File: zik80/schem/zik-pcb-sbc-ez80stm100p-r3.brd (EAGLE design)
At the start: 149.8 x 98.7 mm, 96 parts, among them IC1 7432N, IC2 7404N

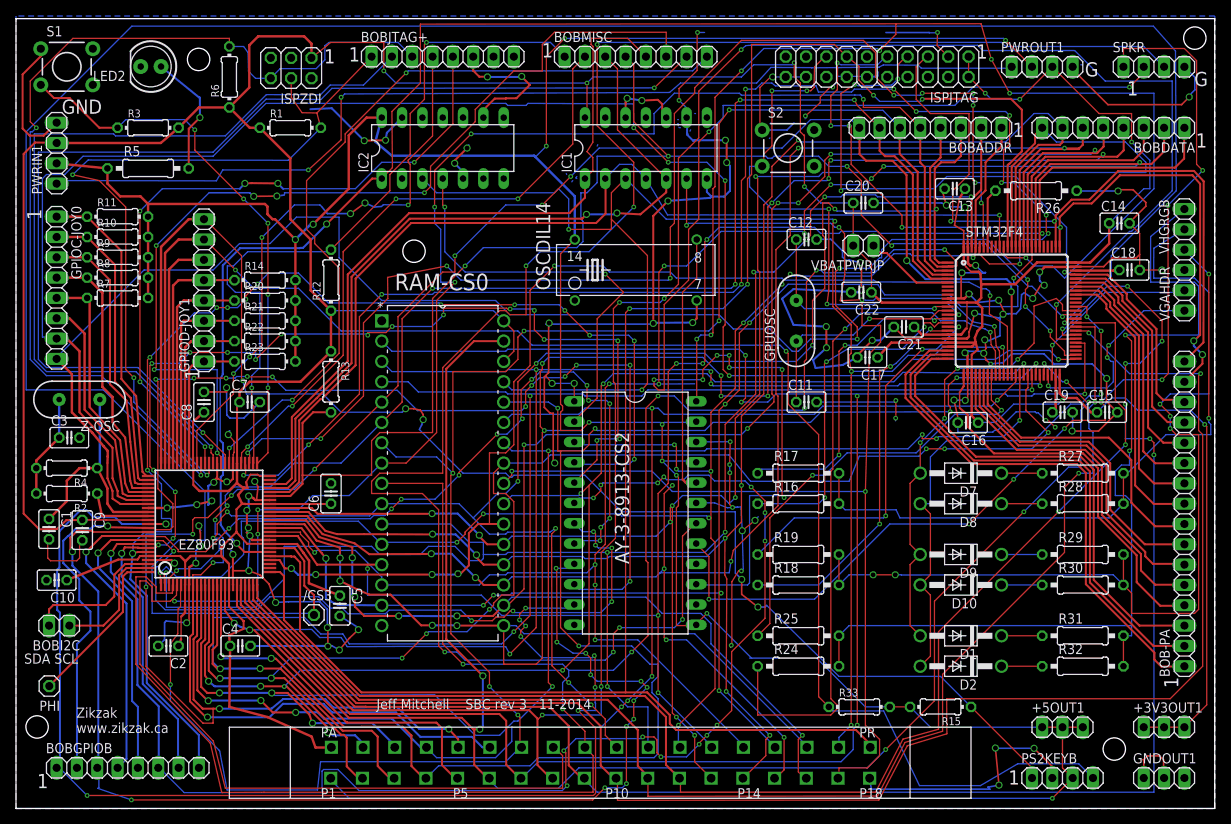
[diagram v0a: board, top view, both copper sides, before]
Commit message: Final(?) rev3 zikzak sbc; created brand new zok atmega644 BoB design and board, WIP
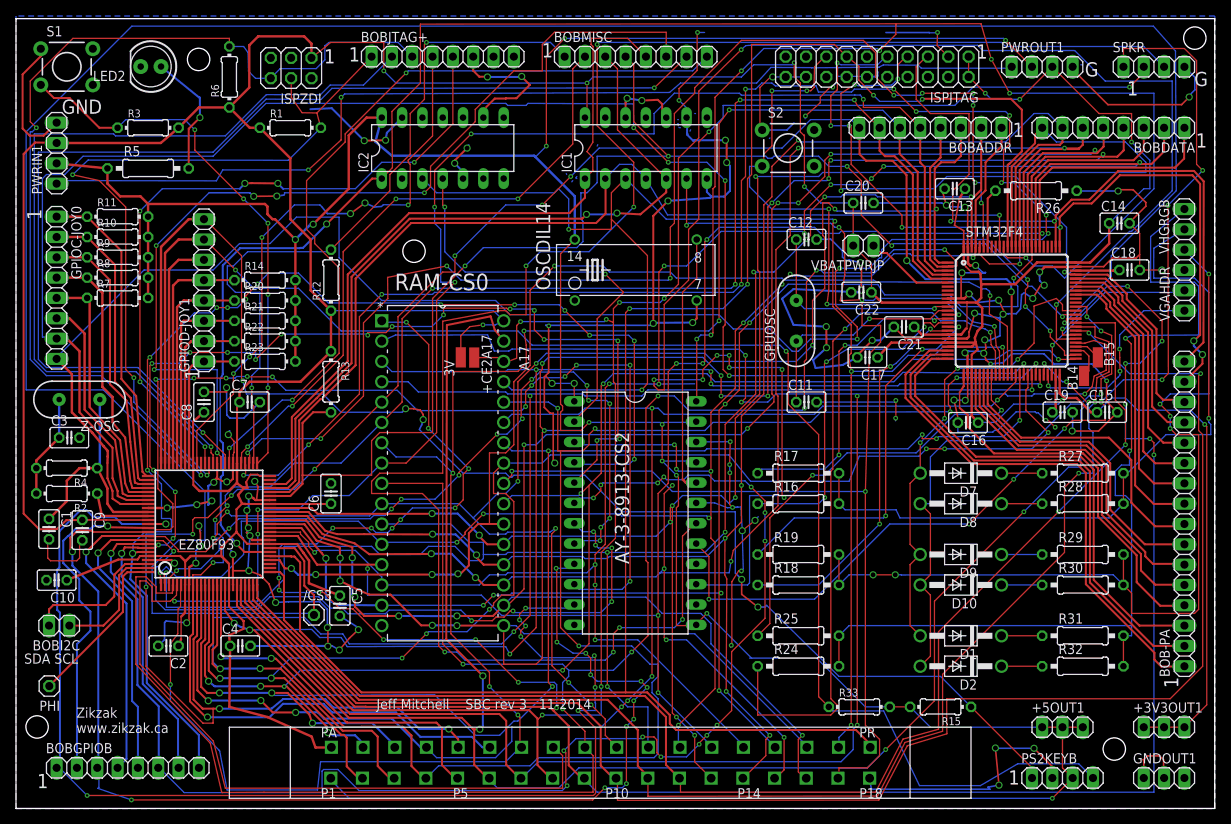
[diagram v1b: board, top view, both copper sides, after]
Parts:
- added +CE2A17, 3V, B14, B15: WIREPADSMD1,27-254, wirepad:SMD1,27-2,54
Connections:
- net +3V3: now also 3V.1; no longer RAM-CS0.30
- net A17: now also +CE2A17.1, RAM-CS0.30
- net A18: now also RAM-CS0.1
- net PB14: now also B14.1
- net PB15: now also B15.1
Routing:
- net A18: track 212.0 -> 315.2 mm, vias 7 -> 22
- net A17: track 251.7 -> 273.9 mm, vias 6 -> 8
- net A15: track 218.2 -> 224.2 mm
- net A16: track 240.9 -> 245.8 mm
- net PB14: track 0.00 -> 4.67 mm
- net PB15: track 0.00 -> 3.33 mm
- net N$28: track 228.4 -> 231.3 mm
- net +3V3: track 655.8 -> 658.3 mm, vias 9 -> 10
- net A20: track 168.3 -> 170.5 mm
- net PC7: track 67.2 -> 68.9 mm
- net A5: track 239.2 -> 240.2 mm
- net PB10: track 26.3 -> 25.5 mm
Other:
- board text added: "A17"

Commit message: Finished up zok atmega bob rev1, and zikzak sbc rev3
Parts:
- renumbered S1 to EZ80-RESET, S2 to STM-RESET
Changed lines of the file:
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@@
 <attribute name="OC_FARNELL" value="unknown" x="100.33" y="10.16" size="1.778" layer="27" display="off"/>
 </element>
-<element name="S1" library="SparkFun-Electromechanical" package="TACTILE-PTH" value="SWITCH-MOMENTARY-2PTH" x="6.35" y="92.71"/>
+<element name="EZ80-RESET" library="SparkFun-Electromechanical" package="TACTILE-PTH" value="SWITCH-MOMENTARY-2PTH" x="6.35" y="92.71"/>
 <element name="R3" library="rcl" package="0204/7" value="10K" x="16.51" y="85.09"/>
 <element name="R2" library="rcl" package="0204/7" value="220 O" x="6.35" y="39.37" rot="R180"/>
@@
 <element name="C18" library="rcl" package="C025-025X050" value="2.2uF" x="139.192" y="67.31"/>
 <element name="C19" library="rcl" package="C025-025X050" value="2.2uF" x="130.81" y="49.53"/>
-<element name="S2" library="SparkFun-Electromechanical" package="TACTILE-PTH" value="SWITCH-MOMENTARY-2PTH" x="96.52" y="82.55"/>
+<element name="STM-RESET" library="SparkFun-Electromechanical" package="TACTILE-PTH" value="SWITCH-MOMENTARY-2PTH" x="96.52" y="82.55"/>
 <element name="VGAHDR" library="pinhead" package="1X06" value="" x="146.05" y="68.58" rot="R90"/>
 <element name="R16" library="rcl" package="0207/10" value="2K" x="97.79" y="38.1"/>
@@
 <contactref element="IC1" pad="7"/>
 <contactref element="IC2" pad="7"/>
-<contactref element="S1" pad="1"/>
+<contactref element="EZ80-RESET" pad="1"/>
 <contactref element="C1" pad="2"/>
 <contactref element="C3" pad="2"/>
@@
 <contactref element="C18" pad="2"/>
 <contactref element="C19" pad="2"/>
-<contactref element="S2" pad="1"/>
+<contactref element="STM-RESET" pad="1"/>
 <contactref element="VGAHDR" pad="3"/>
 <contactref element="R26" pad="1"/>
@@
 </signal>
 <signal name="ZNRST">
-<contactref element="S1" pad="3"/>
+<contactref element="EZ80-RESET" pad="3"/>
 <contactref element="R3" pad="1"/>
 <contactref element="EZ80F93" pad="51"/>
@@
 </signal>
 <signal name="NRST">
-<contactref element="S2" pad="3"/>
+<contactref element="STM-RESET" pad="3"/>
 <contactref element="STM32F4" pad="14"/>
 <contactref element="ISPJTAG" pad="15"/>

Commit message: Text description changes to zikzak SBC rev3 pcb schematic, for clarification on component values etc. No pcb actual changes or schem changes.
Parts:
- R18, R24, R28, R30, R32: value (none) -> 2K
- R19, R25, R27, R29, R31: value (none) -> 1K
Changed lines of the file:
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@@
 <element name="R16" library="rcl" package="0207/10" value="2K" x="97.79" y="38.1"/>
 <element name="R17" library="rcl" package="0207/10" value="1K" x="97.79" y="41.91"/>
-<element name="R18" library="rcl" package="0207/10" value="" x="97.79" y="27.94"/>
-<element name="R19" library="rcl" package="0207/10" value="" x="97.79" y="31.75"/>
-<element name="R24" library="rcl" package="0207/10" value="" x="97.79" y="17.78"/>
-<element name="R25" library="rcl" package="0207/10" value="" x="97.79" y="21.59"/>
+<element name="R18" library="rcl" package="0207/10" value="2K" x="97.79" y="27.94"/>
+<element name="R19" library="rcl" package="0207/10" value="1K" x="97.79" y="31.75"/>
+<element name="R24" library="rcl" package="0207/10" value="2K" x="97.79" y="17.78"/>
+<element name="R25" library="rcl" package="0207/10" value="1K" x="97.79" y="21.59"/>
 <element name="R26" library="rcl" package="0207/10" value="10K" x="127.508" y="77.216" rot="R180"/>
-<element name="R27" library="rcl" package="0207/10" value="" x="133.35" y="41.91"/>
-<element name="R28" library="rcl" package="0207/10" value="" x="133.35" y="38.1"/>
-<element name="R29" library="rcl" package="0207/10" value="" x="133.35" y="31.75"/>
-<element name="R30" library="rcl" package="0207/10" value="" x="133.35" y="27.94"/>
-<element name="R31" library="rcl" package="0207/10" value="" x="133.35" y="21.59"/>
-<element name="R32" library="rcl" package="0207/10" value="" x="133.35" y="17.78"/>
+<element name="R27" library="rcl" package="0207/10" value="1K" x="133.35" y="41.91"/>
+<element name="R28" library="rcl" package="0207/10" value="2K" x="133.35" y="38.1"/>
+<element name="R29" library="rcl" package="0207/10" value="1K" x="133.35" y="31.75"/>
+<element name="R30" library="rcl" package="0207/10" value="2K" x="133.35" y="27.94"/>
+<element name="R31" library="rcl" package="0207/10" value="1K" x="133.35" y="21.59"/>
+<element name="R32" library="rcl" package="0207/10" value="2K" x="133.35" y="17.78"/>
 <element name="VBATPWRJP" library="pinhead" package="1X02" value="" x="105.918" y="70.358" rot="R180"/>
 <element name="C20" library="rcl" package="C025-025X050" value=".1uF" x="105.918" y="75.692"/>
